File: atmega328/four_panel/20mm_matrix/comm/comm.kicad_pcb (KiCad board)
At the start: 2 copper layers, 40 x 40 mm, 12 parts, among them IC5 ATMEGA328-A, P1 CONN15, P2 CONN15, P3 CONN_2X2, P4 CONN_2X2, X5 CER_RESO

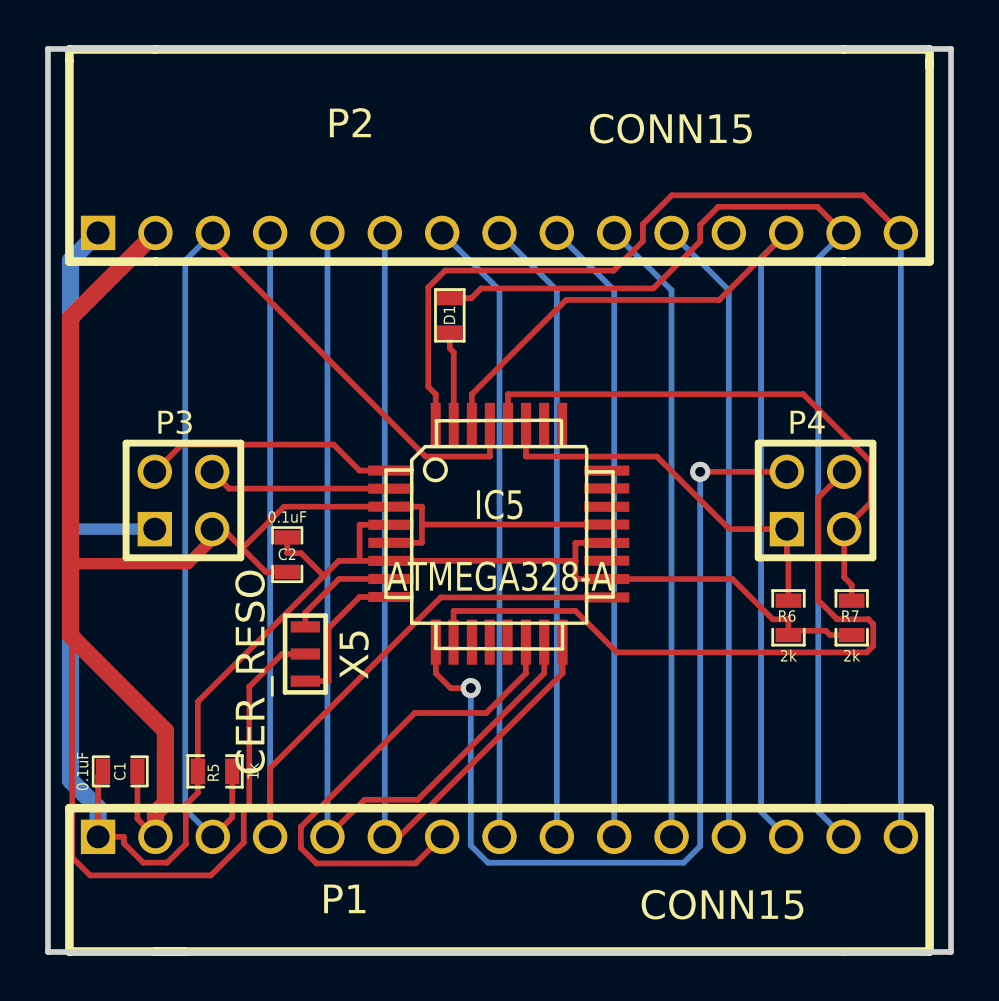
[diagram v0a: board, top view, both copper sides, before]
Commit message: Finished initial verision of four matrix atmega328 based design.
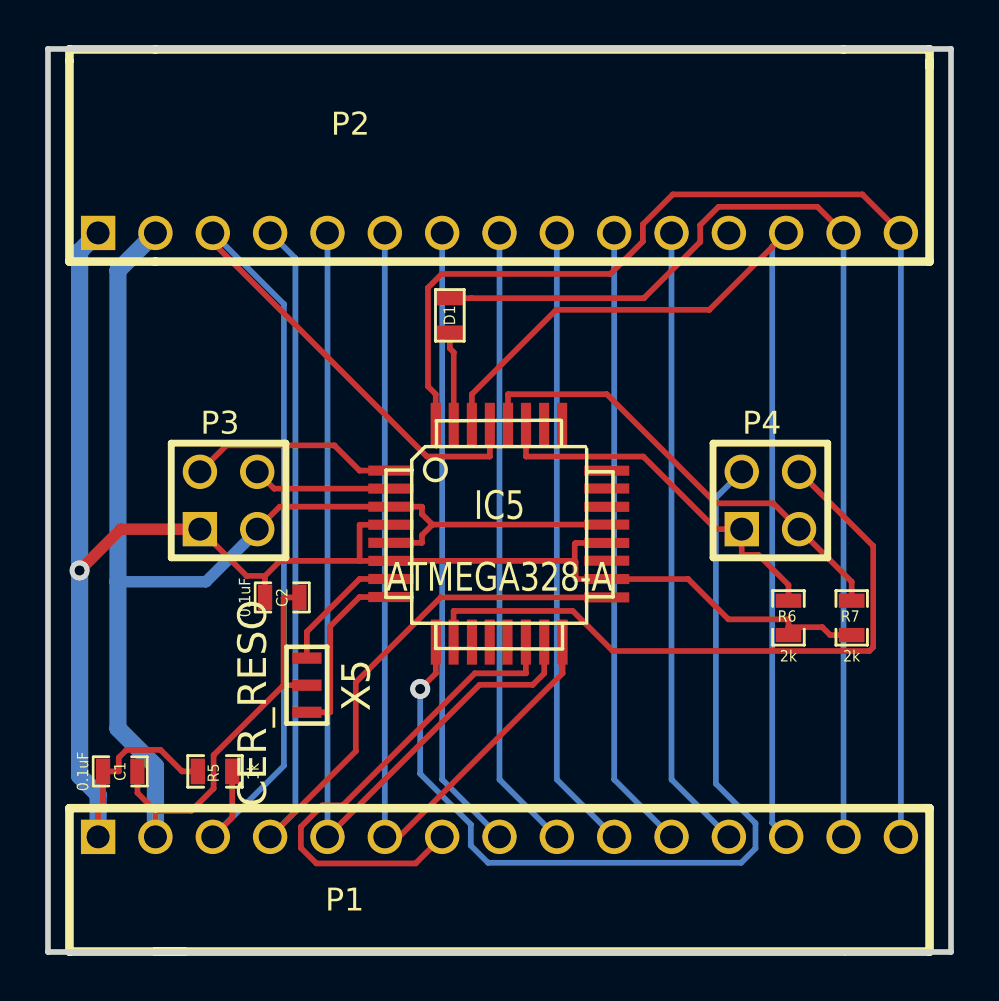
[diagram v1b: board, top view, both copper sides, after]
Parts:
- moved P3 2.00 mm to (58.0, 70.0)
- moved P4 2.00 mm to (82.0, 70.0)
- moved C2 1.91 mm to (60.4, 74.3), turned to 0 degrees
- moved X5 1.38 mm to (61.5, 78.2)
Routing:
- net GND: track 92.8 -> 71.8 mm
- net +5V: track 87.8 -> 80.4 mm, vias 0 -> 1
- net /SCL: track 25.5 -> 20.9 mm
- net /RESET_DRV1: track 11.4 -> 9.40 mm
- net /RESET_DRV2: track 8.22 -> 6.22 mm
- net /RESET_MSTR: track 49.1 -> 50.6 mm
- net /XTAL2: track 6.70 -> 8.06 mm
- net /RESET_DRV4: track 30.9 -> 29.9 mm
- net /SCK: track 47.8 -> 48.8 mm
- net /TX: track 47.7 -> 46.8 mm
- net /XTAL1: track 5.03 -> 5.85 mm
- net /SDA: track 17.5 -> 16.7 mm
- net /RESET_DRV3: track 41.4 -> 41.3 mm, vias 2 -> 1
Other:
- board text added: "BOT"
- board text added: "TOP"

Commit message: Modified atmega328 comm pcb - moved traces out from under osc.
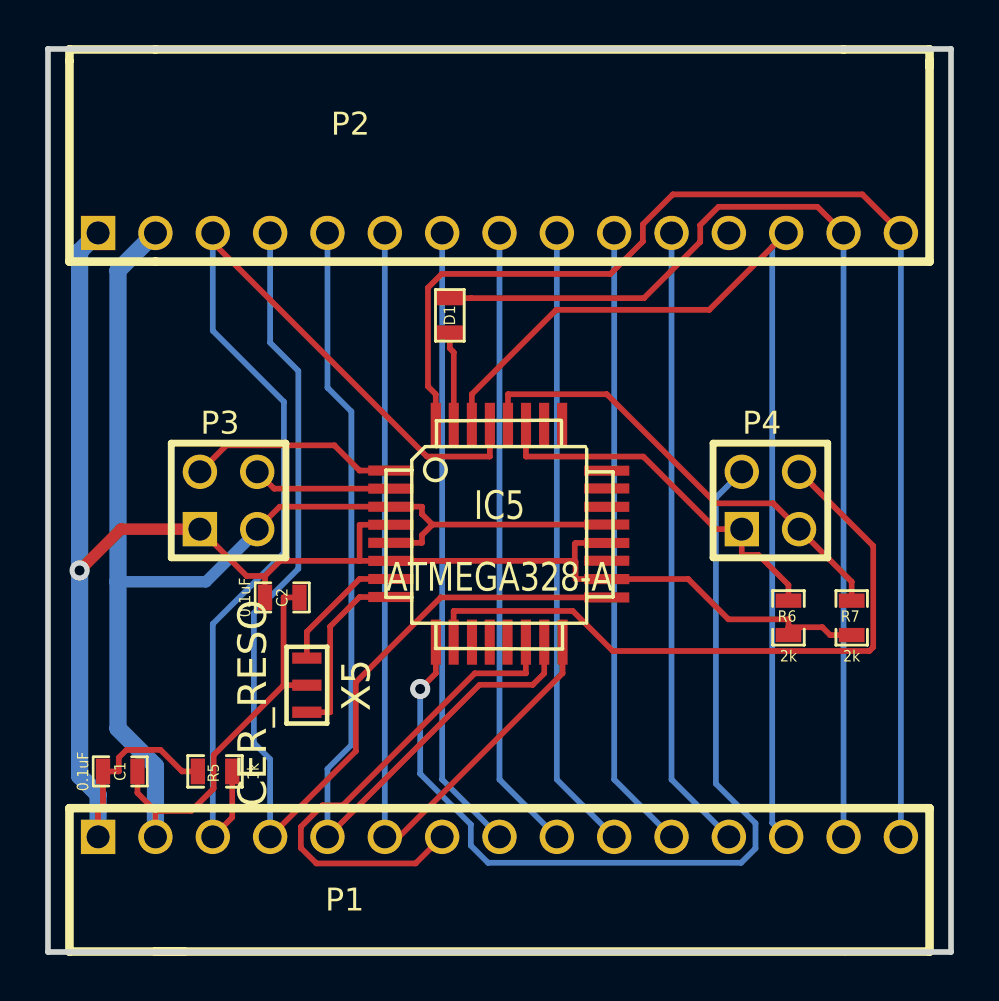
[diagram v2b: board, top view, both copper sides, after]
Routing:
- net /MOSI: track 40.7 -> 41.6 mm
- net /SCK: track 48.8 -> 49.5 mm
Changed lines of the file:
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@@
   (general
     (links 51)
-    (no_connects 47)
+    (no_connects 0)
     (area 49.874999 49.577499 90.125001 90.424501)
     (thickness 1.6)
     (drawings 6)
-    (tracks 190)
+    (tracks 200)
     (zones 0)
     (modules 12)
@@
   (segment (start 67.1755 65.2932) (end 66.832 64.9497) (width 0.254) (layer F.Cu) (net 8))
   (segment (start 67.1755 66.674) (end 67.1755 65.2932) (width 0.254) (layer F.Cu) (net 8))
+  (segment (start 64.92 58.15) (end 64.92 84.9) (width 0.254) (layer B.Cu) (net 9))
   (segment (start 72.794 76.2752) (end 72.794 77.656) (width 0.254) (layer F.Cu) (net 9))
   (segment (start 65.55 84.9) (end 72.794 77.656) (width 0.254) (layer F.Cu) (net 9))
   (segment (start 64.92 84.9) (end 65.55 84.9) (width 0.254) (layer F.Cu) (net 9))
-  (segment (start 64.92 58.15) (end 64.92 84.9) (width 0.254) (layer B.Cu) (net 9))
+  (segment (start 62.38 84.9) (end 62.38 81.89) (width 0.254) (layer B.Cu) (net 10) (status 400000))
+  (segment (start 62.38 65) (end 62.38 58.15) (width 0.254) (layer B.Cu) (net 10) (status 800000))
+  (segment (start 63.44 66.06) (end 62.38 65) (width 0.254) (layer B.Cu) (net 10))
+  (segment (start 63.44 80.83) (end 63.44 66.06) (width 0.254) (layer B.Cu) (net 10))
+  (segment (start 62.38 81.89) (end 63.44 80.83) (width 0.254) (layer B.Cu) (net 10))
   (segment (start 71.9812 76.2752) (end 71.9812 77.656) (width 0.254) (layer F.Cu) (net 10))
-  (segment (start 62.38 58.15) (end 62.38 84.9) (width 0.254) (layer B.Cu) (net 10))
   (segment (start 71.4729 78.1643) (end 71.9812 77.656) (width 0.254) (layer F.Cu) (net 10))
   (segment (start 69.1157 78.1643) (end 71.4729 78.1643) (width 0.254) (layer F.Cu) (net 10))
@@
   (segment (start 83.27 68.73) (end 86.5528 72.0128) (width 0.254) (layer F.Cu) (net 14))
   (segment (start 67.968 76.2752) (end 67.968 74.8944) (width 0.254) (layer F.Cu) (net 14))
+  (segment (start 57.3 84.9) (end 57.3 75.47) (width 0.254) (layer B.Cu) (net 15) (status 400000))
+  (segment (start 57.3 62.48) (end 57.3 58.15) (width 0.254) (layer B.Cu) (net 15) (status 800000))
+  (segment (start 60.451298 65.631298) (end 57.3 62.48) (width 0.254) (layer B.Cu) (net 15))
+  (segment (start 60.451298 72.318702) (end 60.451298 65.631298) (width 0.254) (layer B.Cu) (net 15))
+  (segment (start 57.3 75.47) (end 60.451298 72.318702) (width 0.254) (layer B.Cu) (net 15))
   (segment (start 58.162 84.038) (end 57.3 84.9) (width 0.254) (layer F.Cu) (net 15))
   (segment (start 58.162 82) (end 58.162 84.038) (width 0.254) (layer F.Cu) (net 15))
-  (segment (start 60.4509 61.3009) (end 57.3 58.15) (width 0.254) (layer B.Cu) (net 15))
-  (segment (start 60.4509 81.7491) (end 60.4509 61.3009) (width 0.254) (layer B.Cu) (net 15))
-  (segment (start 57.3 84.9) (end 60.4509 81.7491) (width 0.254) (layer B.Cu) (net 15))
   (segment (start 66.7849 68.0548) (end 69.5733 68.0548) (width 0.254) (layer F.Cu) (net 15))
+  (segment (start 69.5733 66.674) (end 69.5733 68.0548) (width 0.254) (layer F.Cu) (net 15))
+  (segment (start 57.3 58.15) (end 57.3 58.5699) (width 0.254) (layer F.Cu) (net 15))
   (segment (start 57.3 58.5699) (end 66.7849 68.0548) (width 0.254) (layer F.Cu) (net 15))
-  (segment (start 57.3 58.15) (end 57.3 58.5699) (width 0.254) (layer F.Cu) (net 15))
-  (segment (start 69.5733 66.674) (end 69.5733 68.0548) (width 0.254) (layer F.Cu) (net 15))
   (segment (start 82.08 84.28) (end 82.7 84.9) (width 0.254) (layer B.Cu) (net 16))
   (segment (start 82.08 58.77) (end 82.08 84.28) (width 0.254) (layer B.Cu) (net 16))
@@
   (segment (start 68.7757 65.2932) (end 72.5136 61.5553) (width 0.254) (layer F.Cu) (net 16))
   (segment (start 68.7757 66.674) (end 68.7757 65.2932) (width 0.254) (layer F.Cu) (net 16))
-  (segment (start 60.9593 59.2693) (end 59.84 58.15) (width 0.254) (layer B.Cu) (net 17))
-  (segment (start 60.9593 83.7807) (end 60.9593 59.2693) (width 0.254) (layer B.Cu) (net 17))
-  (segment (start 59.84 84.9) (end 60.9593 83.7807) (width 0.254) (layer B.Cu) (net 17))
+  (segment (start 59.84 84.9) (end 59.84 81.46) (width 0.254) (layer B.Cu) (net 17) (status 400000))
+  (segment (start 59.84 63.01) (end 59.84 58.15) (width 0.254) (layer B.Cu) (net 17) (status 800000))
+  (segment (start 61.09 64.26) (end 59.84 63.01) (width 0.254) (layer B.Cu) (net 17))
+  (segment (start 61.09 73.02) (end 61.09 64.26) (width 0.254) (layer B.Cu) (net 17))
+  (segment (start 59.12 74.99) (end 61.09 73.02) (width 0.254) (layer B.Cu) (net 17))
+  (segment (start 59.12 80.74) (end 59.12 74.99) (width 0.254) (layer B.Cu) (net 17))
+  (segment (start 59.84 81.46) (end 59.12 80.74) (width 0.254) (layer B.Cu) (net 17))
   (segment (start 63.6363 81.1037) (end 59.84 84.9) (width 0.254) (layer F.Cu) (net 17))
   (segment (start 63.6363 78.0518) (end 63.6363 81.1037) (width 0.254) (layer F.Cu) (net 17))

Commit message: Modified 4 matrix atmega328 design. Added pin change interrupts and re-routed.
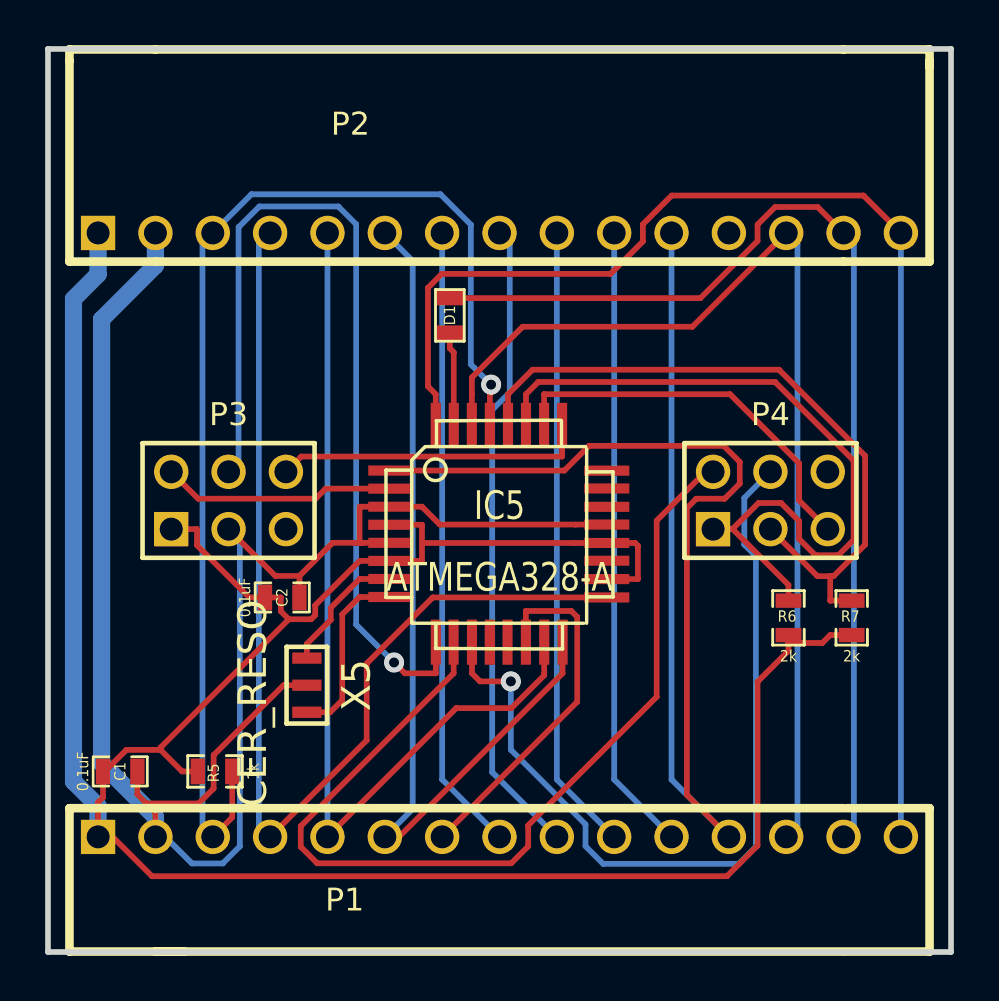
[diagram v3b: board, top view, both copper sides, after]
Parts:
- P3, P4: value CONN_2X2 -> CONN_3X2; footprint PIN_ARRAY_2X2 -> pin_array_3x2
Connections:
- net /EXT_INT renamed /EXT_INT0
- IC5 pad 1: /RESET_DRV1 -> /CS6/EXT_INT1
- IC5 pad 10: /RESET_DRV4 -> /RESET_DRV3
- IC5 pad 11: N-0000025 -> /RESET_DRV4
- IC5 pad 2: /RESET_DRV2 -> /RESET_DRV1
- IC5 pad 25: N-0000030 (its old number) -> /PCINT10/PC2
- IC5 pad 26: N-0000029 -> /PCINT11/PC3
- IC5 pad 9: /RESET_DRV3 -> /RESET_DRV2
- P1 pad 12: /CS6 -> /CS6/EXT_INT1
- P2 pad 11: /CS6 -> /CS6/EXT_INT1
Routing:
- net /CS6/EXT_INT1: track 0.00 -> 63.1 mm
- net +5V: track 80.4 -> 118.2 mm, vias 1 -> 0
- net /RESET_DRV2: track 6.22 -> 40.5 mm, vias 0 -> 1
- net /CS6: track 27.8 -> 0.00 mm
- net /PCINT11/PC3: track 0.00 -> 17.4 mm
- net /SDA: track 16.7 -> 33.7 mm
- net /PCINT10/PC2: track 0.00 -> 13.9 mm
- net GND: track 71.8 -> 83.6 mm
- net /SCL: track 20.9 -> 30.8 mm
- net /RESET_DRV4: track 29.9 -> 37.4 mm, vias 0 -> 1
- net /CS1: track 22.1 -> 16.0 mm
- net /RESET_MSTR: track 50.6 -> 52.4 mm, vias 0 -> 1
- net /RESET_DRV3: track 41.3 -> 42.7 mm, vias 1 -> 0
- net /MISO: track 39.0 -> 40.0 mm
- net /SCK: track 49.5 -> 48.5 mm
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
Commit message: Created gerber files and BOM for 4-matrix atmega328 and max6960 PCBs.
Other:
- board text added: "4-Matrix Atmega328 Comm v0.1 www.iorodeo.com"
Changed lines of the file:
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@@
     (area 49.874999 49.577499 90.125001 90.424501)
     (thickness 1.6)
-    (drawings 6)
+    (drawings 7)
     (tracks 262)
     (zones 0)
@@
     (visible_elements FFFFFF7F)
     (pcbplotparams
-      (layerselection 3178497)
+      (layerselection 284196865)
       (usegerberextensions true)
       (excludeedgelayer true)
@@
       (outputformat 1)
       (mirror false)
-      (drillshape 1)
+      (drillshape 0)
       (scaleselection 1)
-      (outputdirectory ""))
+      (outputdirectory gerber_v0p1/))
   )
   (net 0 "")
@@
   (module HEADER_BOT (layer F.Cu)
     (at 70 84.9)
-    (fp_text reference P1 (at -6.858 2.794) (layer F.SilkS)
+    (fp_text reference P1 (at -17.5744 3.9111) (layer F.SilkS)
       (effects (font (size 1.016 1.016) (thickness 0.2032)))
     )
@@
   (module HEADER_TOP (layer F.Cu)
     (at 70 58.15)
-    (fp_text reference P2 (at -6.604 -4.826) (layer F.SilkS)
+    (fp_text reference P2 (at -17.549 -7.0706) (layer F.SilkS)
       (effects (font (size 1.016 1.016) (thickness 0.2032)))
     )
@@
   (module TQFP32 (layer F.Cu)
     (at 70 71.5)
-    (fp_text reference IC5 (at 0 -1.27) (layer F.SilkS)
-      (effects (font (size 1.27 1.016) (thickness 0.2032)))
-    )
-    (fp_text value ATMEGA328-A (at 0 1.905) (layer F.SilkS)
+    (fp_text reference IC5 (at -4.9252 -5.1679) (layer F.SilkS)
+      (effects (font (size 1.016 1.016) (thickness 0.2032)))
+    )
+    (fp_text value ATMEGA328-A (at 0 1.905) (layer F.SilkS) hide
       (effects (font (size 1.27 1.016) (thickness 0.2032)))
     )
@@
     (tags "Resonator, Ceramic")
     (fp_text reference X5 (at 0 -2.19964 270) (layer F.SilkS)
-      (effects (font (size 1.27 1.27) (thickness 0.2032)))
-    )
-    (fp_text value CER_RESO (at 0.8001 2.4003 270) (layer F.SilkS)
+      (effects (font (size 1.016 1.016) (thickness 0.2032)))
+    )
+    (fp_text value CER_RESO (at 0.8001 2.4003 270) (layer F.SilkS) hide
       (effects (font (size 1.27 1.27) (thickness 0.2032)))
     )
@@
     )
   )
+  (gr_text "4-Matrix Atmega328 Comm v0.1\nwww.iorodeo.com" (at 69.7992 52.5272) (layer B.SilkS)
+    (effects (font (size 1.016 1.016) (thickness 0.2032)) (justify mirror))
+  )
   (gr_text BOT (at 86.9 88.7) (layer B.SilkS)
